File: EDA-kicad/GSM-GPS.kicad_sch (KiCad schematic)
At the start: 2 parts, among them J2 SIM-G85D1160022HHR, U1 EG25GGC-128-SGNS

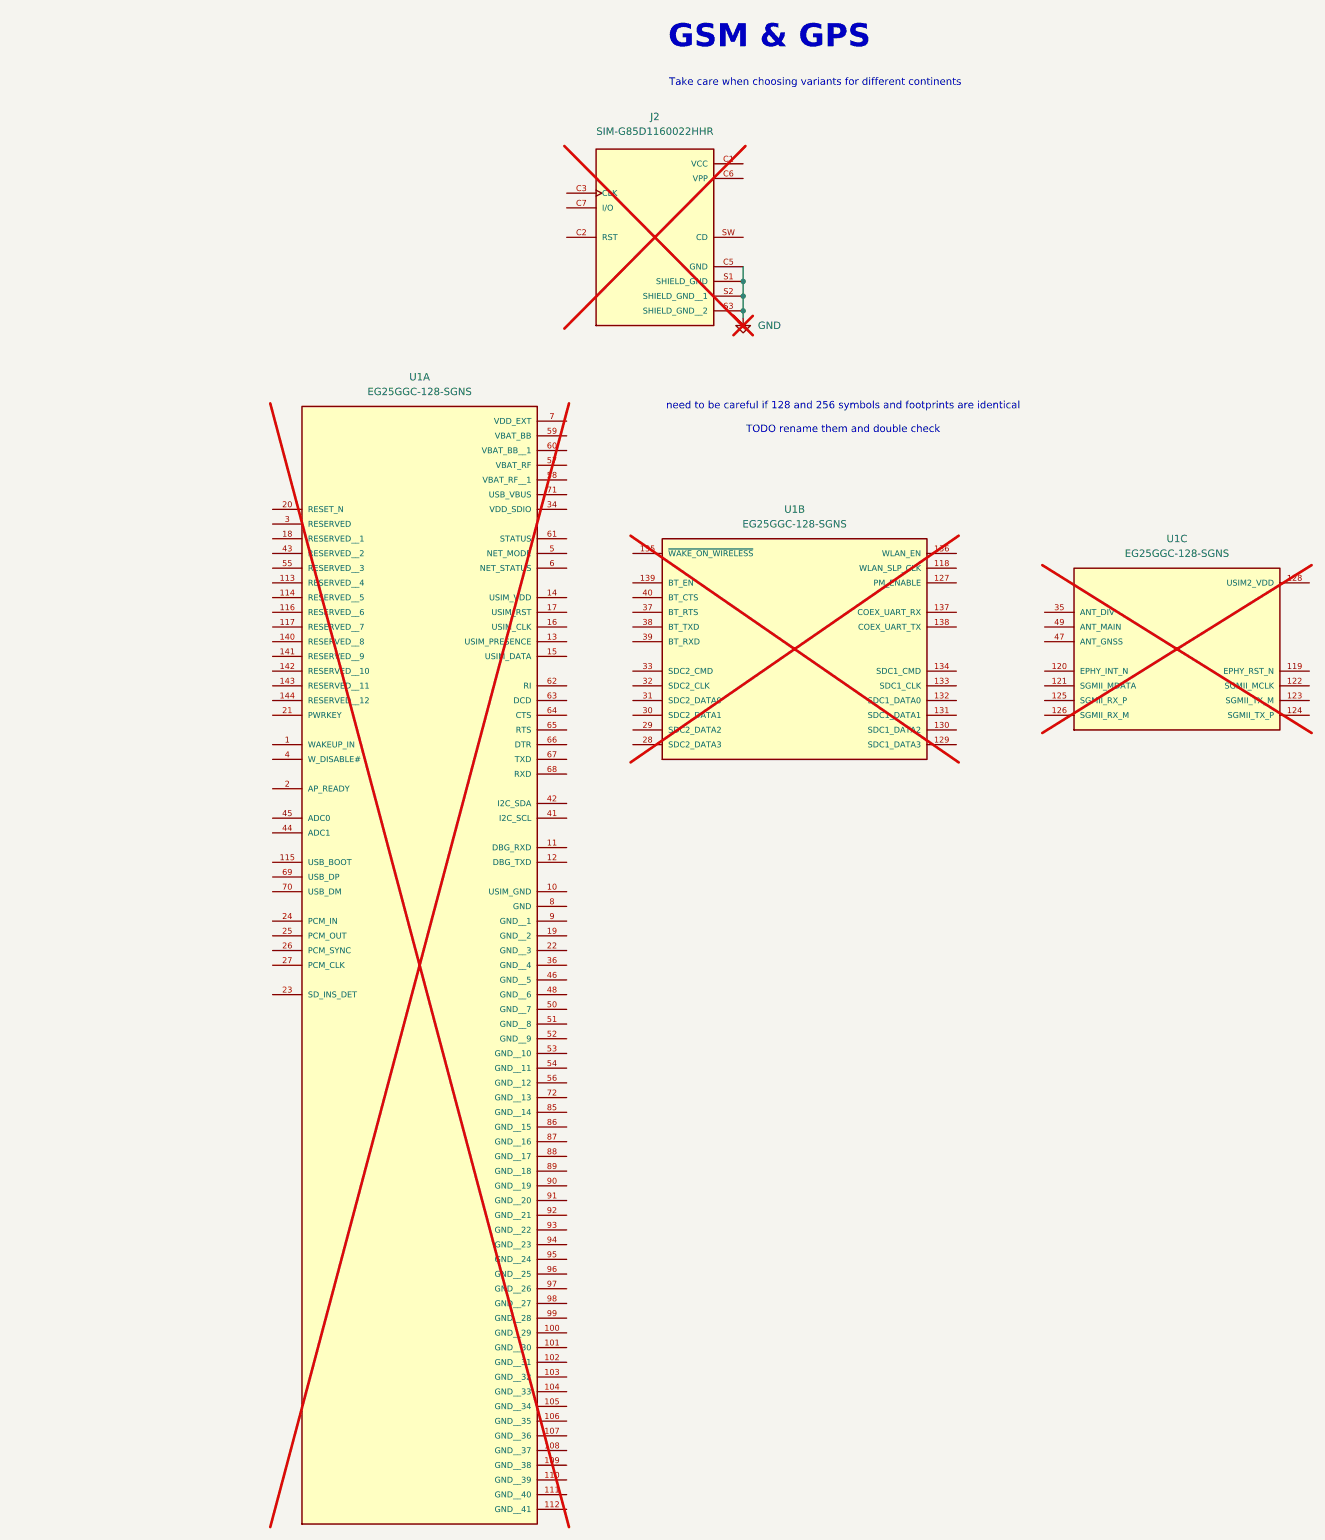
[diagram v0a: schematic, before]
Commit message: Wired sim card to GNSS
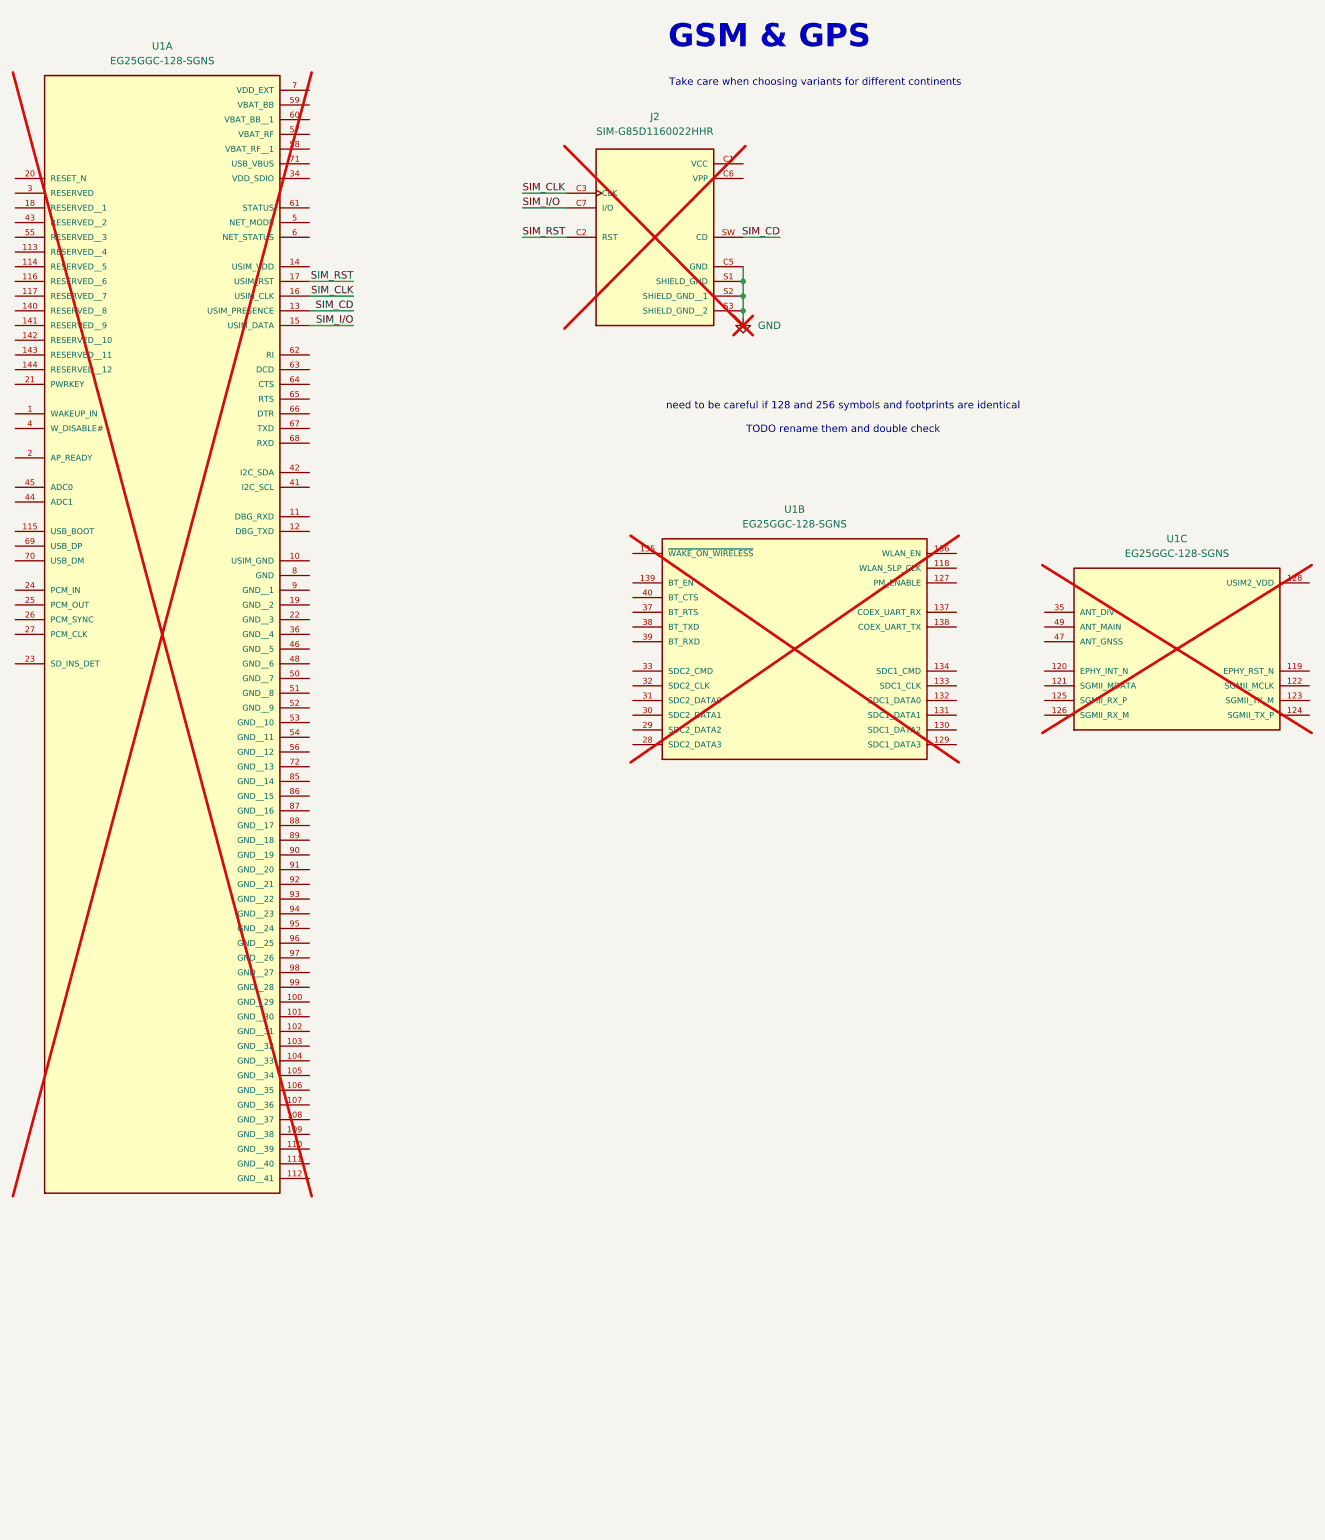
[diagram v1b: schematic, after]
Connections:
- net SIM_RST: now reaches J2.C2 (RST)
- net SIM_RST: now also U1.17 (USIM_RST)
- net SIM_CLK: now reaches J2.C3 (CLK)
- net SIM_CLK: now also U1.16 (USIM_CLK)
- net SIM_I/O: now reaches J2.C7 (I/O)
- net SIM_I/O: now also U1.15 (USIM_DATA)
- net SIM_CD: now reaches J2.SW (CD)
- net SIM_CD: now also U1.13 (USIM_PRESENCE)
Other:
- moved on the sheet: U1A
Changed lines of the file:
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@@
+	(wire
+		(pts
+			(xy 113.03 48.26) (xy 120.65 48.26)
+		)
+		(stroke
+			(width 0)
+			(type default)
+		)
+	)
 	(wire
 		(pts
@@
 	(wire
 		(pts
+			(xy 113.03 45.72) (xy 120.65 45.72)
+		)
+		(stroke
+			(width 0)
+			(type default)
+		)
+	)
+	(wire
+		(pts
+			(xy 83.82 63.5) (xy 76.2 63.5)
+		)
+		(stroke
+			(width 0)
+			(type default)
+		)
+	)
+	(wire
+		(pts
+			(xy 83.82 66.04) (xy 76.2 66.04)
+		)
+		(stroke
+			(width 0)
+			(type default)
+		)
+	)
+	(wire
+		(pts
 			(xy 151.13 67.31) (xy 151.13 66.04)
 		)
@@
 	(wire
 		(pts
+			(xy 113.03 53.34) (xy 120.65 53.34)
+		)
+		(stroke
+			(width 0)
+			(type default)
+		)
+	)
+	(wire
+		(pts
+			(xy 157.48 53.34) (xy 151.13 53.34)
+		)
+		(stroke
+			(width 0)
+			(type default)
+		)
+	)
+	(wire
+		(pts
 			(xy 151.13 63.5) (xy 151.13 66.04)
 		)
@@
 			(width 0)
 			(type default)
+		)
+	)
+	(wire
+		(pts
+			(xy 83.82 68.58) (xy 76.2 68.58)
+		)
+		(stroke
+			(width 0)
+			(type default)
+		)
+	)
+	(wire
+		(pts
+			(xy 83.82 60.96) (xy 76.2 60.96)
+		)
+		(stroke
+			(width 0)
+			(type default)
+		)
+	)
+	(label "SIM_RST"
+		(at 83.82 60.96 180)
+		(effects
+			(font
+				(size 1.27 1.27)
+			)
+			(justify right bottom)
+		)
+	)
+	(label "SIM_CLK"
+		(at 83.82 63.5 180)
+		(effects
+			(font
+				(size 1.27 1.27)
+			)
+			(justify right bottom)
+		)
+	)
+	(label "SIM_RST"
+		(at 113.03 53.34 0)
+		(effects
+			(font
+				(size 1.27 1.27)
+			)
+			(justify left bottom)
+		)
+	)
+	(label "SIM_I{slash}O"
+		(at 113.03 48.26 0)
+		(effects
+			(font
+				(size 1.27 1.27)
+			)
+			(justify left bottom)
+		)
+	)
+	(label "SIM_CLK"
+		(at 113.03 45.72 0)
+		(effects
+			(font
+				(size 1.27 1.27)
+			)
+			(justify left bottom)
+		)
+	)
+	(label "SIM_CD"
+		(at 157.48 53.34 180)
+		(effects
+			(font
+				(size 1.27 1.27)
+			)
+			(justify right bottom)
+		)
+	)
+	(label "SIM_CD"
+		(at 83.82 66.04 180)
+		(effects
+			(font
+				(size 1.27 1.27)
+			)
+			(justify right bottom)
+		)
+	)
+	(label "SIM_I{slash}O"
+		(at 83.82 68.58 180)
+		(effects
+			(font
+				(size 1.27 1.27)
+			)
+			(justify right bottom)
 		)
 	)
@@
 	(symbol
 		(lib_id "SPIRIT-components:EG25GGC-128-SGNS")
-		(at 95.25 123.19 0)
+		(at 50.8 66.04 0)
 		(unit 1)
 		(exclude_from_sim no)
@@
 		(fields_autoplaced yes)
 		(property "Reference" "U1"
-			(at 95.25 77.47 0)
+			(at 50.8 20.32 0)
 			(effects
 				(font
@@
 		)
 		(property "Value" "EG25GGC-128-SGNS"
-			(at 95.25 80.01 0)
+			(at 50.8 22.86 0)
 			(effects
 				(font
@@
 		)
 		(property "Footprint" "SPIRIT-footprints:XCVR_EG25GGC-128-SGNS"
-			(at 95.25 123.19 0)
+			(at 50.8 66.04 0)
 			(effects
 				(font
@@
 		)
 		(property "Datasheet" ""
-			(at 95.25 123.19 0)
+			(at 50.8 66.04 0)
 			(effects
 				(font
@@
 		)
 		(property "Description" ""
-			(at 95.25 123.19 0)
+			(at 50.8 66.04 0)
 			(effects
 				(font
@@
 		)
 		(property "MF" "Quectel"
-			(at 95.25 123.19 0)
+			(at 50.8 66.04 0)
 			(effects
 				(font
@@
 		)
 		(property "Description_1" "Quectel EG25-G is an LTE Cat 4 module optimized specially for M2M and IoT applications. Adopting the 3GPP Rel. 11 LTE technology, it delivers 150Mbps downlink and 50Mbps uplink data rates"
-			(at 95.25 123.19 0)
+			(at 50.8 66.04 0)
 			(effects
 				(font
@@
 		)
 		(property "Package" "Custom Quectel"
-			(at 95.25 123.19 0)
+			(at 50.8 66.04 0)
 			(effects
 				(font
@@
 		)
 		(property "Price" "None"
-			(at 95.25 123.19 0)
+			(at 50.8 66.04 0)
 			(effects
 				(font
@@
 		)
 		(property "MP" "EG25GGC-128-SGNS"
-			(at 95.25 123.19 0)
+			(at 50.8 66.04 0)
 			(effects
 				(font
@@
 		)
 		(property "Availability" "In Stock"
-			(at 95.25 123.19 0)
-			(effects
-				(font
+			(at 50.8 66.04 0)
+			(effects
+				(font
